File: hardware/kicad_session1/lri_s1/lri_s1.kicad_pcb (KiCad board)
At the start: 2 copper layers, 43 parts, among them J1 USB_C_Receptacle_USB2.0_16P, Q3 CSD17318Q2, SW1 MJTP1230, SW2 MJTP1230, U1 STM32F042F6P6, U2 LP5912-3.3DRV, U3 ICM-20602, U4 BMP280

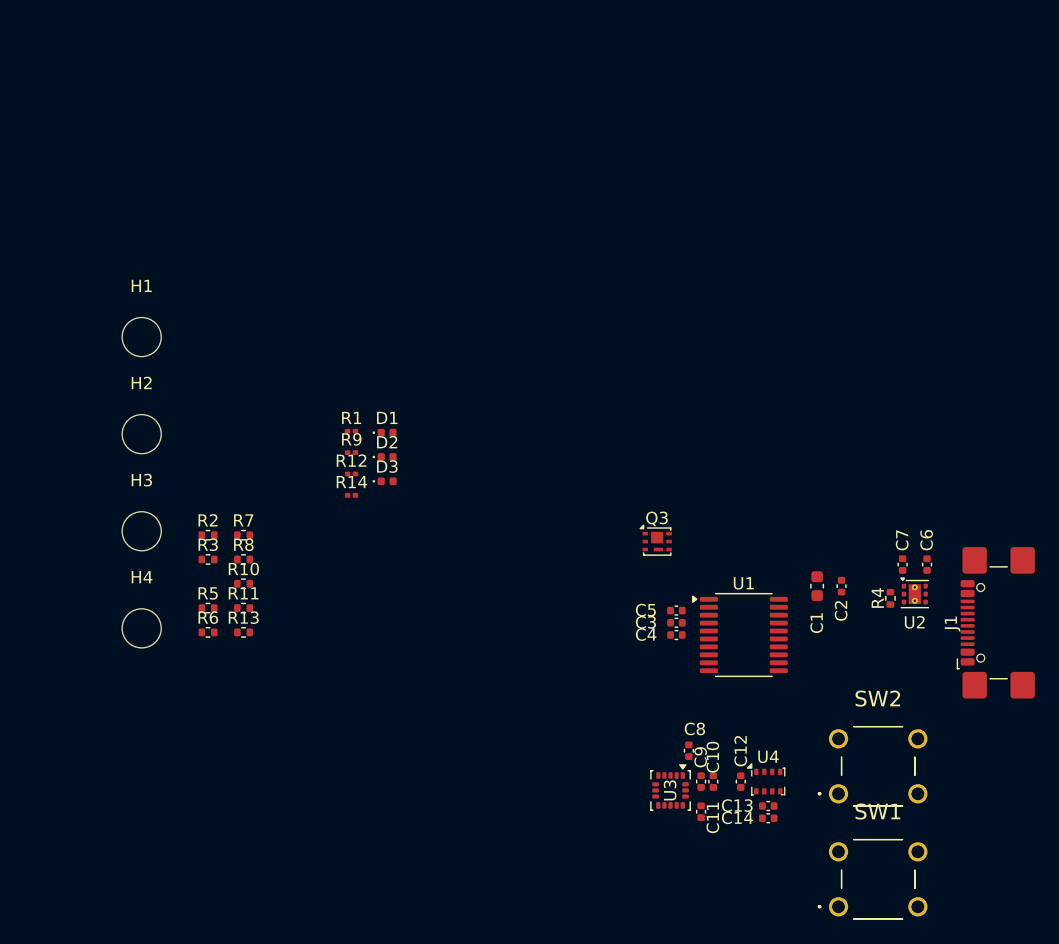
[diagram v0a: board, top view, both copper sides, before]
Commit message: Simplified LED FET circuit, general BOM consolidation. First instance of layout, need to redo.
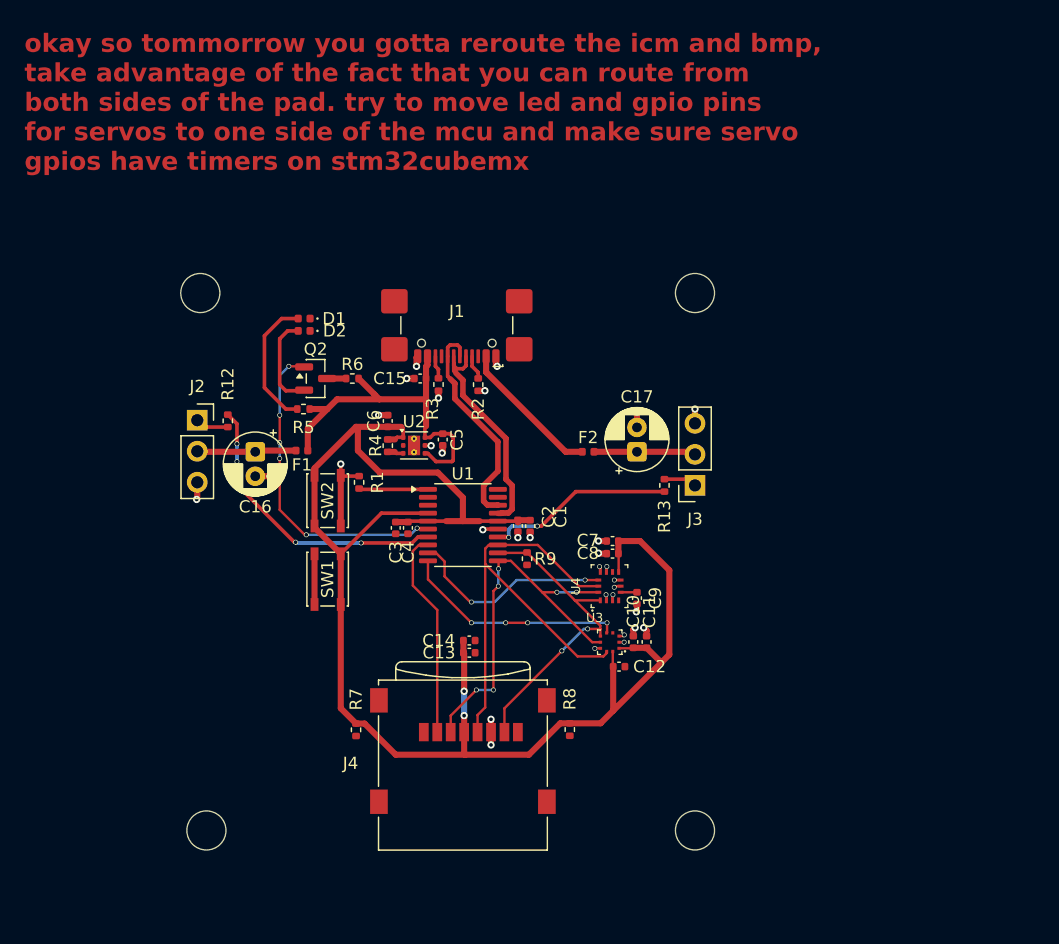
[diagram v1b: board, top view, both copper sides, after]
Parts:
- removed D3: RED, LED_SMD:LED_0402_1005Metric
- removed Q3: CSD17318Q2, Package_SON:Texas_DQK
- removed R10, R11: 100, Resistor_SMD:R_0402_1005Metric
- removed R14: 10k, Resistor_SMD:R_0201_0603Metric
- added C15: 10u, Capacitor_SMD:C_0402_1005Metric, F.Cu at (139.5, 84.0)
- added C16: 100u, Capacitor_THT:CP_Radial_D5.0mm_P2.00mm, F.Cu at (126.0, 90.0)
- added C17: 100u, Capacitor_THT:CP_Radial_D5.0mm_P2.00mm, F.Cu at (157.2, 90.0)
- added F1: 1A, Fuse:Fuse_0402_1005Metric, F.Cu at (129.8, 89.9)
- added F2: 1A, Fuse:Fuse_0402_1005Metric, F.Cu at (153.2, 90.0)
- added J2: CTRL1, Connector_PinSocket_2.54mm:PinSocket_1x03_P2.54mm_Vertical, F.Cu at (121.3, 87.4)
- added J3: CTRL2, Connector_PinSocket_2.54mm:PinSocket_1x03_P2.54mm_Vertical, F.Cu at (162.0, 92.8)
- added J4: Micro_SD_Card, Connector_Card:microSD_HC_Wuerth_693072010801, F.Cu at (143.0, 114.5)
- added Q2: T2N7002AK, Package_TO_SOT_SMD:SOT-23, F.Cu at (130.9, 84.0)
- C1: value 4.7u -> 10u; footprint Capacitor_SMD:C_0603_1608Metric -> Capacitor_SMD:C_0402_1005Metric
- C10: value 2.2u -> 10u
- C13: value 100n -> 10u
- C14: value 2.2u -> 100n
- C5: value 100n -> 1u
- C7: value 1u -> 10u
- C9: value 100n -> 10n
- R1, R9: value 10k -> 5.1k; footprint Resistor_SMD:R_0201_0603Metric -> Resistor_SMD:R_0402_1005Metric
- R12: value 10k -> 1k; footprint Resistor_SMD:R_0201_0603Metric -> Resistor_SMD:R_0402_1005Metric
- R13: value 100 -> 1k
- R7: value 1k -> 5.1k
- R8: value 100 -> 5.1k
- SW1, SW2: value MJTP1230 -> SW_Push; footprint lib:MJTP1230 -> Button_Switch_SMD:SW_SPST_PTS810
- U3: value ICM-20602 -> BMP390; footprint Package_LGA:LGA-16_3x3mm_P0.5mm_LayoutBorder3x5y -> lib:BMP390_LGA_2x2x0.75
- U4: value BMP280 -> ICM-42688-P; footprint Package_LGA:Bosch_LGA-8_2x2.5mm_P0.65mm_ClockwisePinNumbering -> lib:ICM-42688_LGA_0.91x2.50x3.00
- moved J1 52.2 mm to (142.5, 78.5), turned to 180 degrees
- moved SW1 51.3 mm to (131.9, 100.4), turned to -90 degrees
- moved SW2 50.0 mm to (131.9, 94.0), turned to -90 degrees
- moved H4 48.2 mm to (162.0, 121.0)
- moved H2 46.7 mm to (162.0, 77.0)
- moved C6 45.7 mm to (136.8, 87.5)
- moved R4 43.0 mm to (136.8, 89.5)
- moved U2 42.8 mm to (139.0, 89.5)
- moved R13 36.5 mm to (159.5, 92.8), turned to 90 degrees
- moved R8 30.1 mm to (151.8, 112.7), turned to -90 degrees
- moved C14 28.5 mm to (143.5, 105.5), turned to 180 degrees
- moved C13 27.5 mm to (143.5, 106.4), turned to 180 degrees
- moved C2 27.0 mm to (147.5, 96.1)
- moved R2 25.3 mm to (144.2, 84.5), turned to -90 degrees
- moved H3 25.1 mm to (122.0, 121.0)
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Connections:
- C11 pad 1: Net-(U3-REGOUT) -> GND
- C11 pad 2: GND -> +3V3
- C5 pad 1: GND -> VBUS
- C5 pad 2: +3V3 -> GND
- C6 pad 1: VBUS -> +3V3
- C7 pad 1: +3V3 -> GND
- C7 pad 2: GND -> +3V3
- R1 pad 1: +3V3 -> GND
- R1 pad 2: Net-(SW2-A) -> Net-(R1-Pad2)
- R12 pad 1: GND -> /GPIO1
- R13 pad 1: Net-(Q2-G) -> /GPIO2
- R13 pad 2: /MCU_PY1 -> Net-(J3-Pin_1)
- R5 pad 2: +3V3 -> VBUS
- R7 pad 1: Net-(Q2-D) (its old number) -> +3V3
- R7 pad 2: VBUS -> Net-(J4-DAT2)
- R8 pad 1: Net-(Q3-G) -> +3V3
- R8 pad 2: /MCU_PY1 -> Net-(J4-DAT1)
- R9 pad 1: GND -> +3V3
- R9 pad 2: Net-(Q3-G) -> /SPI1_MISO
- SW1 pad 1: GND -> +3V3
- SW2 pad 1: GND -> Net-(R1-Pad2)
- SW2 pad 2: GND -> +3V3
- U1 pad 1: +3V3 -> GND
- U1 pad 14: unconnected-(U1-PB1-Pad14) -> /GPIO2
- U1 pad 6: /MCU_LED -> /LED
- U1 pad 7: /MCU_PY1 -> /GPIO1
- U1 pad 8: unconnected-(U1-PA2-Pad8) -> /SD_~{CS}
- U3 pad 10: GND -> +3V3
- U3 pad 3: /SPI1_MOSI -> GND
- U3 pad 4: /SPI1_MISO -> /SPI1_MOSI
- U3 pad 5: /ICM_~{CS} -> /SPI1_MISO
- U3 pad 6: unconnected-(U3-INT-Pad6) -> /BMP_~{CS}
- U4 pad 1: GND -> /SPI1_MISO
- U4 pad 2: /BMP_~{CS} -> GND
- U4 pad 3: /SPI1_MOSI -> GND
- U4 pad 4: /SPI1_MISO -> unconnected-(U4-INT1-Pad4)
- U4 pad 5: /SPI1_SCK -> +3V3
- U4 pad 6: +3V3 -> GND
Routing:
- net +3V3: track 0.00 -> 131.1 mm, vias 0 -> 2
- net VBUS: track 0.00 -> 41.9 mm
- net /SPI1_SCK: track 0.00 -> 39.4 mm
- net GND: track 0.00 -> 32.4 mm, vias 0 -> 31
- net /SPI1_MOSI: track 0.00 -> 32.2 mm, vias 0 -> 6
- net /LED: track 0.00 -> 26.6 mm, vias 0 -> 6
- net /SPI1_MISO: track 0.00 -> 26.3 mm, vias 0 -> 2
- net /GPIO1: track 0.00 -> 23.9 mm, vias 0 -> 4
- net /BMP_~{CS}: track 0.00 -> 18.5 mm, vias 0 -> 4
- net /USB_D+: track 0.00 -> 18.0 mm
- net /USB_D-: track 0.00 -> 18.0 mm
- net /SD_~{CS}: track 0.00 -> 17.1 mm
- net /ICM_~{CS}: track 0.00 -> 17.1 mm, vias 0 -> 2
- net /GPIO2: track 0.00 -> 15.6 mm, vias 0 -> 2
- net Net-(D1-A): track 0.00 -> 11.0 mm
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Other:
- rule pad_to_mask_clearance: 0 -> 0.05
- board text added: "okay so tommorrow you gotta reroute the icm and bmp, take advantage of the fact that you can route from both sides of the pad. try to move led and gpio pins for servos to one side of the mcu and make sure servo gpios have timers on stm32cubemx"

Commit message: Finished tutorial flight computer PCB, awaiting backcheck + merge.
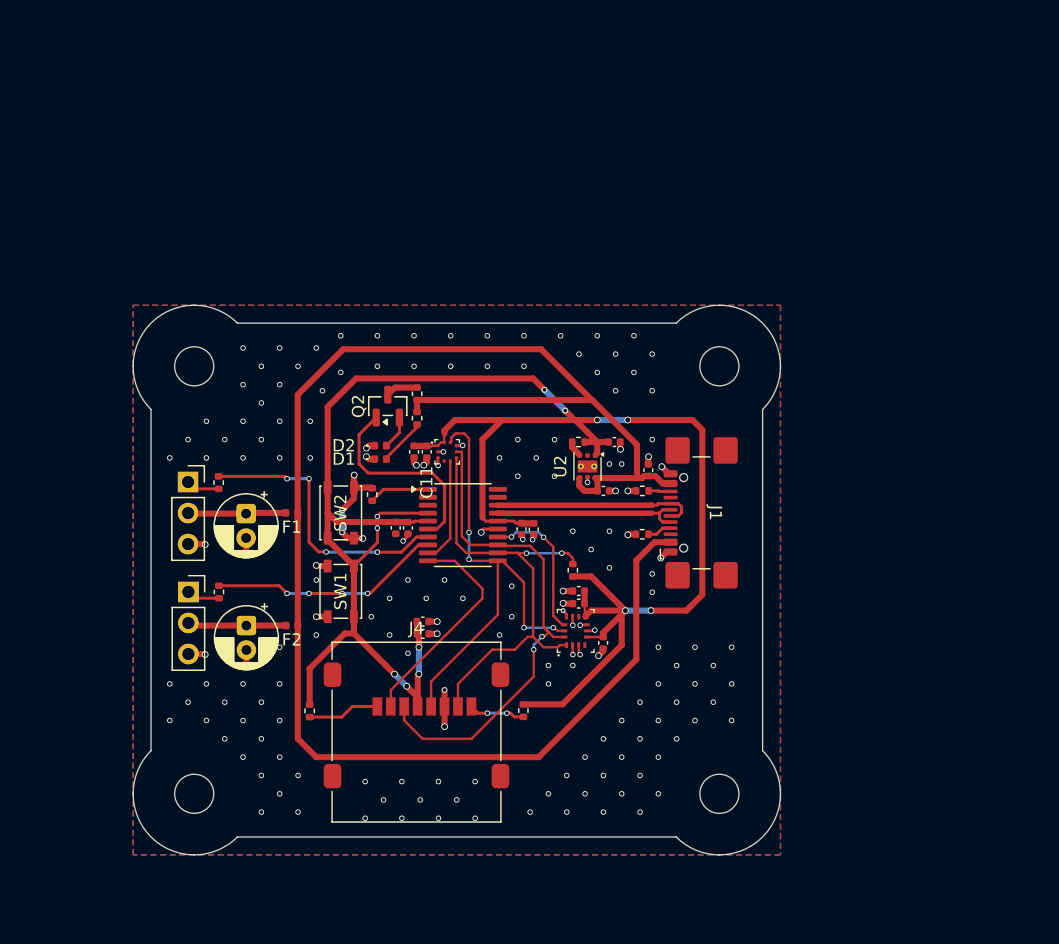
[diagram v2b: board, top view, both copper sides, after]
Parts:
- removed the C10 at (156.9, 105.6)
- J4: footprint Connector_Card:microSD_HC_Wuerth_693072010801 -> Connector_Card:microSD_HC_Molex_47219-2001
- moved J3 42.4 mm to (120.5, 101.5), turned to 0 degrees
- moved R13 37.5 mm to (123.0, 101.5), turned to -90 degrees
- moved C17 35.0 mm to (125.3, 104.2), turned to -90 degrees
- moved F2 28.1 mm to (129.0, 104.2), turned to 180 degrees
- moved J1 26.8 mm to (163.7, 95.0), turned to 90 degrees
- moved C10 24.6 mm to (139.0, 90.0), turned to 90 degrees
- moved C11 23.6 mm to (140.0, 90.0), turned to 90 degrees
- moved U3 20.5 mm to (141.7, 90.0), turned to 0 degrees
- moved C15 20.1 mm to (158.2, 91.5), turned to 90 degrees
- moved R3 18.8 mm to (157.7, 93.2), turned to 180 degrees
- moved C6 18.6 mm to (155.4, 89.2), turned to 0 degrees
- moved R2 18.2 mm to (157.7, 96.8), turned to 180 degrees
- moved R4 15.6 mm to (152.5, 89.2), turned to 180 degrees
- moved U2 14.3 mm to (153.2, 91.2), turned to -90 degrees
- moved C5 13.8 mm to (154.5, 93.2), turned to 0 degrees
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- renumbered C11 to C10, C12 to C11
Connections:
- U1 pad 10: /BMP_~{CS} -> /SD_~{CS}
- U1 pad 11: /SPI1_MOSI -> /SPI1_SCK
- U1 pad 13: /SPI1_SCK -> /SPI1_MOSI
- U1 pad 14: /GPIO2 -> /ICM_~{CS}
- U1 pad 8: /SD_~{CS} -> /GPIO2
- U1 pad 9: /ICM_~{CS} -> /BMP_~{CS}
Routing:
- net VBUS: track 41.9 -> 131.9 mm
- net +3V3: track 131.1 -> 174.8 mm, vias 2 -> 12
- net /SPI1_MISO: track 26.3 -> 38.2 mm
- net /LED: track 26.6 -> 16.7 mm, vias 6 -> 0
- net /BMP_~{CS}: track 18.5 -> 8.65 mm, vias 4 -> 0
- net /SPI1_MOSI: track 32.2 -> 41.7 mm, vias 6 -> 2
- net Net-(D1-A): track 11.0 -> 3.98 mm
- net Net-(J4-DAT2): track 0.00 -> 5.91 mm
- net /ICM_~{CS}: track 17.1 -> 12.0 mm
- net Net-(D2-A): track 7.76 -> 2.74 mm
- net Net-(J4-DAT1): track 0.00 -> 4.61 mm, vias 0 -> 2
- net GND: track 32.4 -> 36.3 mm, vias 31 -> 176
- net /GPIO2: track 15.6 -> 19.0 mm, vias 2 -> 4
- net /USB_D-: track 18.0 -> 15.7 mm
- net Net-(R1-Pad2): track 6.60 -> 8.55 mm, vias 1 -> 4
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- added copper zone on B.Cu, net GND
- added copper zone on F.Cu, net GND
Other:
- board outline added: 53 x 45 mm
- rule pad_to_mask_clearance: 0.05 -> 0
- board text removed: "okay so tommorrow you gotta reroute the icm and bmp, take advantage of the fact that you can route from both sides of the pad. try to move led and gpio pins for servos to one side of the mcu and make sure servo gpios have timers on stm32cubemx"

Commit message: Cleaned up layout
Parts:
- added G***: LOGO, lib:logo, F.Cu at (128.5, 83.5)
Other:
- board text added: "+5V"
- board text added: "BAROMETER"
- board text added: "BOOT"
- board text added: "GND"
- board text added: "IMU"
- board text added: "LDO"
- board text added: "LRI EXAMPLE BOARD"
- board text added: "MCU"
- board text added: "NRST"
- board text added: "PWM"
- board text added: "PWR"
- board text added: "SD CARD"
- board text added: "USB-C"
